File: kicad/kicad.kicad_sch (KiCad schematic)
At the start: 0 parts

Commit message: added kicad logic files
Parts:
- added A1: RaspberryPi_Pico_W, Module:RaspberryPi_Pico_W_SMD_HandSolder, symbol MCU_Module:RaspberryPi_Pico_W
- added R1: 500, Resistor_SMD:R_0402_1005Metric, symbol Device:R
- added R2: 750, Resistor_SMD:R_0402_1005Metric, symbol Device:R
- added U1, U2, U3: SEN-13723, SEN-13723:MODULE_SEN-13723, symbol SEN-13723:SEN-13723
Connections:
- new net +3V0: A1.35 (ADC_VREF), R1.1, R2.2, U1.1 (VS), U2.1 (VS), U3.1 (VS)
- new net +5V: A1.40 (VBUS), R1.2
- new net ADC0: A1.31 (GPIO26_ADC0), U3.3 (SIG)
- new net ADC1: A1.32 (GPIO27_ADC1), U1.3 (SIG)
- new net ADC2: A1.34 (GPIO28_ADC2), U2.3 (SIG)
- new net GNDREF: A1.13 (GND), A1.18 (GND), A1.23 (GND), A1.28 (GND), A1.3 (GND), A1.33 (AGND), A1.38 (GND), A1.8 (GND), R2.1, U1.2 (GND), U2.2 (GND), U3.2 (GND)
- no-connect marks 0 -> 46
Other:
- added sheet Battery Management (untitled.kicad_sch)

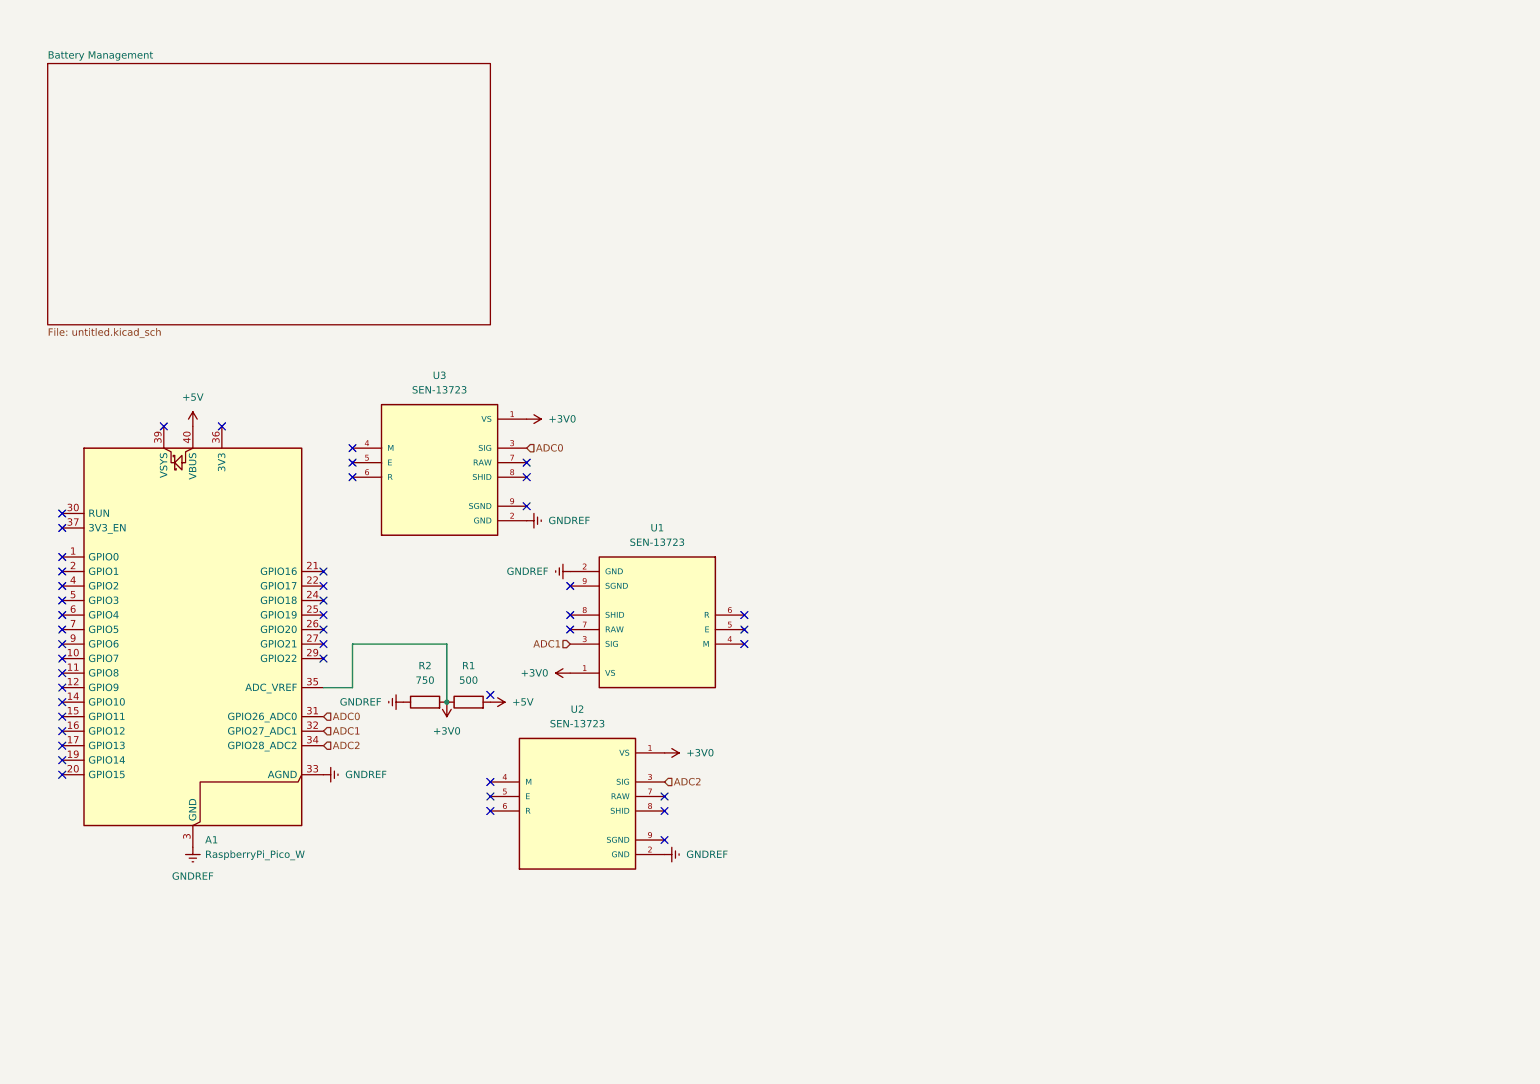
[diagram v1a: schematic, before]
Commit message: added motor driver and motors to schematic; left space for future motors with encoders
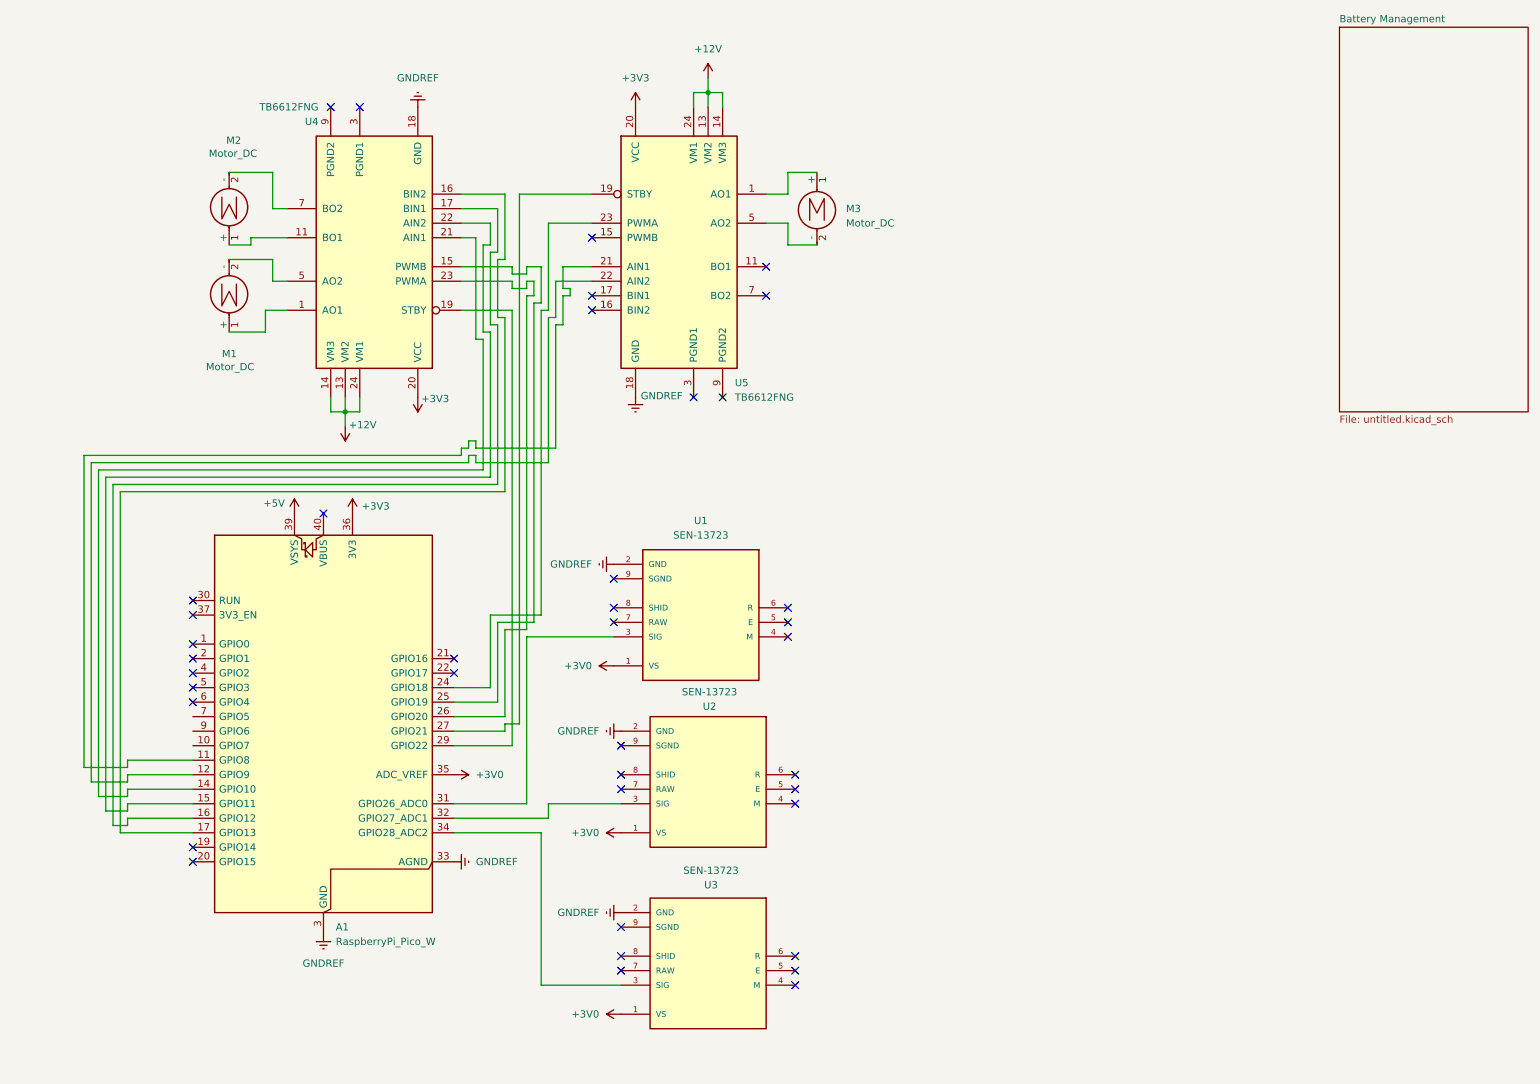
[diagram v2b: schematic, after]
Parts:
- removed R1: 500, Resistor_SMD:R_0402_1005Metric, symbol Device:R
- removed R2: 750, Resistor_SMD:R_0402_1005Metric, symbol Device:R
- added M1, M2, M3: Motor_DC, symbol Motor:Motor_DC
- added U4, U5: TB6612FNG, Package_SO:SSOP-24_5.3x8.2mm_P0.65mm, symbol Driver_Motor:TB6612FNG
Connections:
- net +5V: now also A1.39 (VSYS); no longer A1.40 (VBUS)
- net GNDREF: now also U4.18 (GND), U5.18 (GND)
- net at A1.11 (GPIO8): now also U5.21 (AIN1)
- net at A1.12 (GPIO9): now also U5.22 (AIN2)
- net at A1.14 (GPIO10): now also U4.21 (AIN1)
- net at A1.15 (GPIO11): now also U4.22 (AIN2)
- net at A1.16 (GPIO12): now also U4.17 (BIN1)
- net at A1.17 (GPIO13): now also U4.16 (BIN2)
- net at A1.24 (GPIO18): now also U5.23 (PWMA)
- net at A1.25 (GPIO19): now also U4.15 (PWMB)
- net at A1.26 (GPIO20): now also U4.23 (PWMA)
- net at A1.27 (GPIO21): now also U5.19 (STBY)
- net at A1.29 (GPIO22): now also U4.19 (STBY)
- net +3V3: now reaches A1.36 (3V3)
- net +3V3: now also U4.20 (VCC), U5.20 (VCC)
- net ADC0: no longer names the net of A1.31 (GPIO26_ADC0)
- net ADC0: now also U1.3 (SIG); no longer U3.3 (SIG)
- net ADC1: no longer names the net of A1.32 (GPIO27_ADC1)
- net ADC1: now also U2.3 (SIG); no longer U1.3 (SIG)
- net ADC2: no longer names the net of A1.34 (GPIO28_ADC2)
- net ADC2: now also U3.3 (SIG); no longer U2.3 (SIG)
- new net: M1.1 (+), U4.1 (AO1), U4.2 (AO1)
- new net: M1.2 (-), U4.5 (AO2), U4.6 (AO2)
- new net: M3.1 (+), U5.1 (AO1), U5.2 (AO1)
- new net: M3.2 (-), U5.5 (AO2), U5.6 (AO2)
- new net: U4.10 (PGND2), U4.9 (PGND2)
- new net: M2.1 (+), U4.11 (BO1), U4.12 (BO1)
- new net: U4.3 (PGND1), U4.4 (PGND1)
- new net: M2.2 (-), U4.7 (BO2), U4.8 (BO2)
- new net: U5.10 (PGND2), U5.9 (PGND2)
- new net: U5.11 (BO1), U5.12 (BO1)
- new net: U5.3 (PGND1), U5.4 (PGND1)
- new net: U5.7 (BO2), U5.8 (BO2)
- new net +12V: U4.13 (VM2), U4.14 (VM3), U4.24 (VM1), U5.13 (VM2), U5.14 (VM3), U5.24 (VM1)
- no-connect marks 46 -> 39
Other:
- moved on the sheet: A1, U1, U2, U3

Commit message: kicad schematic mostly finished; struggling with footprints; updated pico code to match schematic
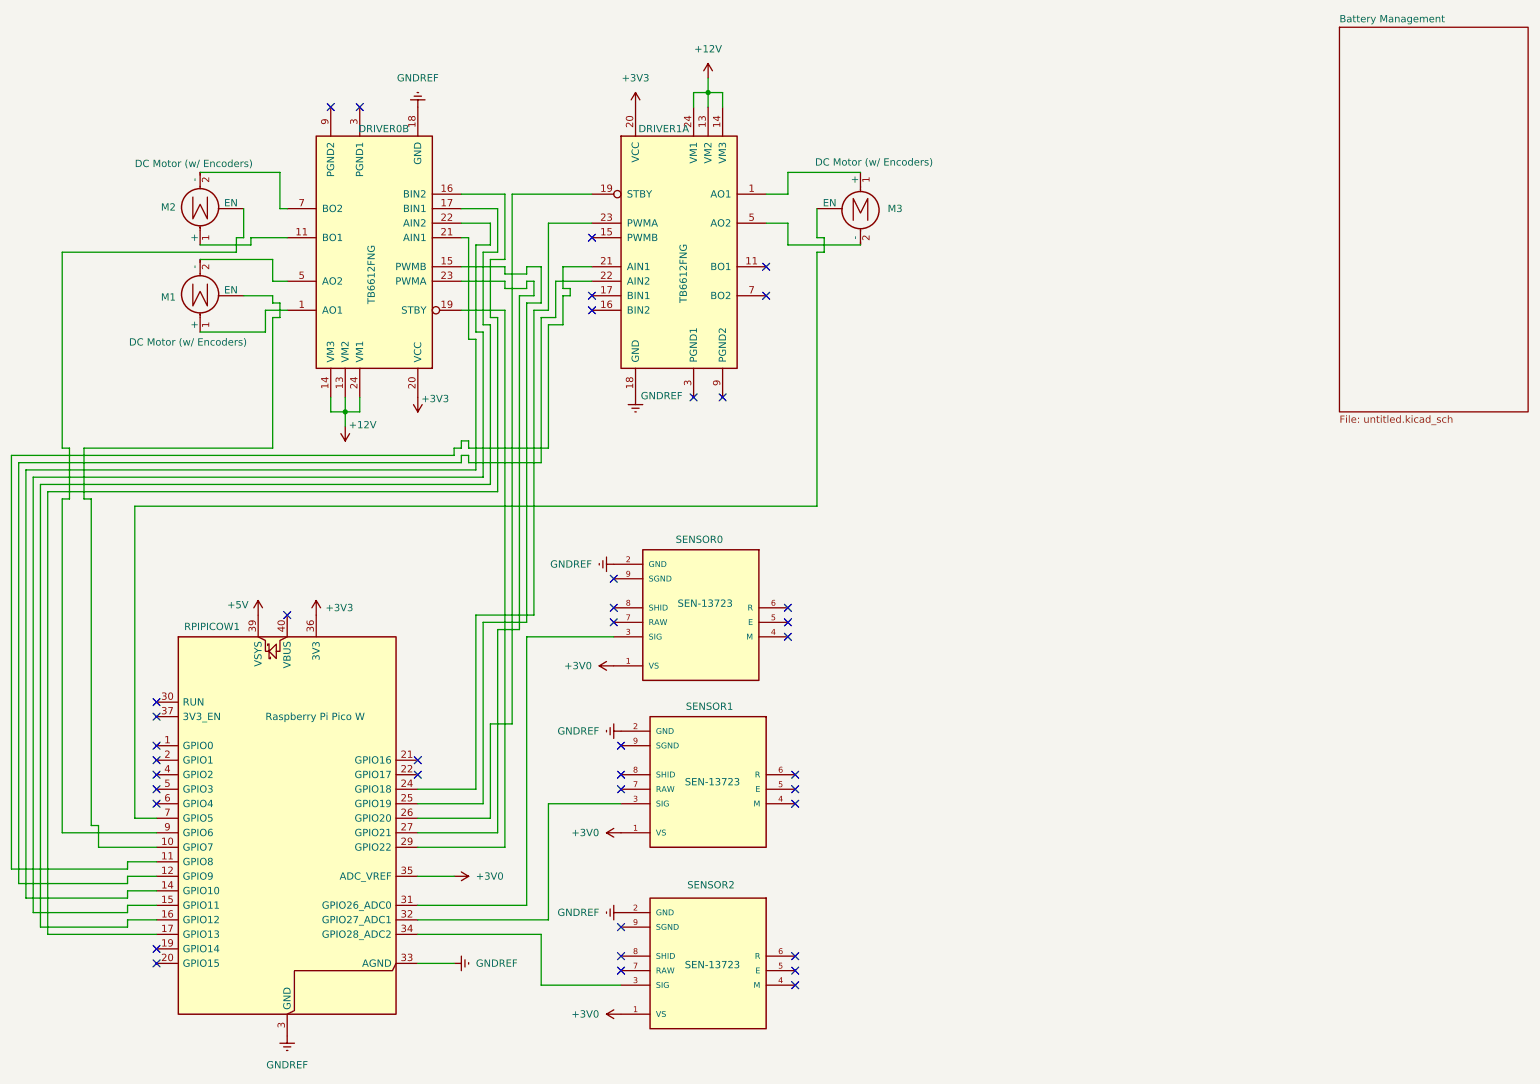
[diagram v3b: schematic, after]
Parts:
- DRIVER0: renamed from U4; footprint Package_SO:SSOP-24_5.3x8.2mm_P0.65mm -> Connector_PinHeader_2.54mm:PinHeader_1x08_P2.54mm_Vertical
- DRIVER1: renamed from U5; footprint Package_SO:SSOP-24_5.3x8.2mm_P0.65mm -> Connector_PinHeader_2.54mm:PinHeader_1x08_P2.54mm_Vertical
- M1, M2, M3: value Motor_DC -> DC Motor (w/ Encoders); footprint (none) -> Connector_PinHeader_1.00mm:PinHeader_1x03_P1.00mm_Vertical
- RPIPICOW1: renamed from A1; value RaspberryPi_Pico_W -> Raspberry Pi Pico W; footprint Module:RaspberryPi_Pico_W_SMD_HandSolder -> Module:RaspberryPi_Pico_Common_THT
- SENSOR0: renamed from U1; footprint SEN-13723:MODULE_SEN-13723 -> Connector_PinSocket_2.54mm:PinSocket_1x03_P2.54mm_Vertical
- SENSOR1: renamed from U2; footprint SEN-13723:MODULE_SEN-13723 -> Connector_PinSocket_2.54mm:PinSocket_1x03_P2.54mm_Vertical
- SENSOR2: renamed from U3; footprint SEN-13723:MODULE_SEN-13723 -> Connector_PinSocket_2.54mm:PinSocket_1x03_P2.54mm_Vertical
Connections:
- net at DRIVER0.23 (PWMA): now also RPIPICOW1.27 (GPIO21); no longer RPIPICOW1.26 (GPIO20)
- net at RPIPICOW1.10 (GPIO7): now also M1. (EN)
- net at DRIVER1.19 (STBY): now also RPIPICOW1.26 (GPIO20); no longer RPIPICOW1.27 (GPIO21)
- net at RPIPICOW1.7 (GPIO5): now also M3. (EN)
- net at RPIPICOW1.9 (GPIO6): now also M2. (EN)
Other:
- moved on the sheet: RPIPICOW1

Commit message: pcb mostly finished
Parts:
- removed DRIVER0: TB6612FNG, Connector_PinHeader_2.54mm:PinHeader_1x08_P2.54mm_Vertical, symbol Driver_Motor:TB6612FNG
- added DRIVER2: TB6612FNG, Breakout_Board:Motor_Driver_Breakout, symbol Driver_Motor:TB6612FNG
- DRIVER1: footprint Connector_PinHeader_2.54mm:PinHeader_1x08_P2.54mm_Vertical -> Breakout_Board:Motor_Driver_Breakout
- M1, M2, M3: footprint Connector_PinHeader_1.00mm:PinHeader_1x03_P1.00mm_Vertical -> Breakout_Board:Untitled_1
- SENSOR0, SENSOR1, SENSOR2: footprint Connector_PinSocket_2.54mm:PinSocket_1x03_P2.54mm_Vertical -> Breakout_Board:Untitled_1
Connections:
- net +12V: now also DRIVER1.16 (VM1), DRIVER2.16 (VM1); no longer DRIVER1.13 (VM2), DRIVER1.14 (VM3), DRIVER1.24 (VM1)
- net +3V3: now also DRIVER1.15 (Vcc), DRIVER2.15 (Vcc); no longer DRIVER1.20 (VCC)
- net GNDREF: now also DRIVER1.14 (GND), DRIVER2.14 (GND); no longer DRIVER1.18 (GND)
- net at RPIPICOW1.7 (GPIO5): now also M3.3 (EN); no longer M3. (EN)
- net at RPIPICOW1.10 (GPIO7): now also M1.3 (EN); no longer M1. (EN)
- net at M1.1 (+): now also DRIVER2.13 (AO1), DRIVER2.2 (AO1)
- net at M1.2 (-): now also DRIVER2.12 (BO1), DRIVER2.6 (AO2)
- net at M2.1 (+): now also DRIVER2.10 (BO1), DRIVER2.12 (BO1)
- net at RPIPICOW1.25 (GPIO19): now also DRIVER2.7 (PWMB)
- net at RPIPICOW1.17 (GPIO13): now also DRIVER2.6 (AO2)
- net at RPIPICOW1.16 (GPIO12): now also DRIVER2.5 (BIN1)
- net at RPIPICOW1.29 (GPIO22): now also DRIVER2.4 (STBY)
- net at RPIPICOW1.14 (GPIO10): now also DRIVER2.3 (AIN1)
- net at RPIPICOW1.15 (GPIO11): now also DRIVER2.2 (AO1)
- net at RPIPICOW1.27 (GPIO21): now also DRIVER2.1 (PWMA)
- net at M2.2 (-): now also DRIVER2.11 (BO2), DRIVER2.8 (BO2)
- net at RPIPICOW1.11 (GPIO8): now also DRIVER1.3 (AIN1); no longer DRIVER1.21 (AIN1)
- net at RPIPICOW1.12 (GPIO9): now also DRIVER1.2 (AO1); no longer DRIVER1.22 (AIN2)
- net at RPIPICOW1.24 (GPIO18): now also DRIVER1.1 (PWMA); no longer DRIVER1.23 (PWMA)
- net at RPIPICOW1.26 (GPIO20): now also DRIVER1.4 (STBY); no longer DRIVER1.19 (STBY)
- net at RPIPICOW1.9 (GPIO6): now also M2.3 (EN); no longer M2. (EN)
- net at DRIVER1.10 (BO1): now also DRIVER1.12 (BO1); no longer DRIVER1.9 (PGND2)
- net at DRIVER1.11 (BO2): now also DRIVER1.8 (BO2); no longer DRIVER1.12 (BO1)
- net at DRIVER1.7 (PWMB): no longer DRIVER1.8 (BO2)
- new net: DRIVER1.13 (AO1), DRIVER1.2 (AO1), M3.1 (+)
- new net: DRIVER1.12 (BO1), DRIVER1.6 (AO2), M3.2 (-)
- now unconnected: DRIVER1.5 (AO2), DRIVER1.6 (AO2)
